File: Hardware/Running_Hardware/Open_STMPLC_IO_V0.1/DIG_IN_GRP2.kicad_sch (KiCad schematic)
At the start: 68 parts, among them J3 Screw_Terminal_01x04, J8 Screw_Terminal_01x04, U12 6N137, U20 6N137, U21 6N137, U22 6N137, U23 6N137, U24 6N137

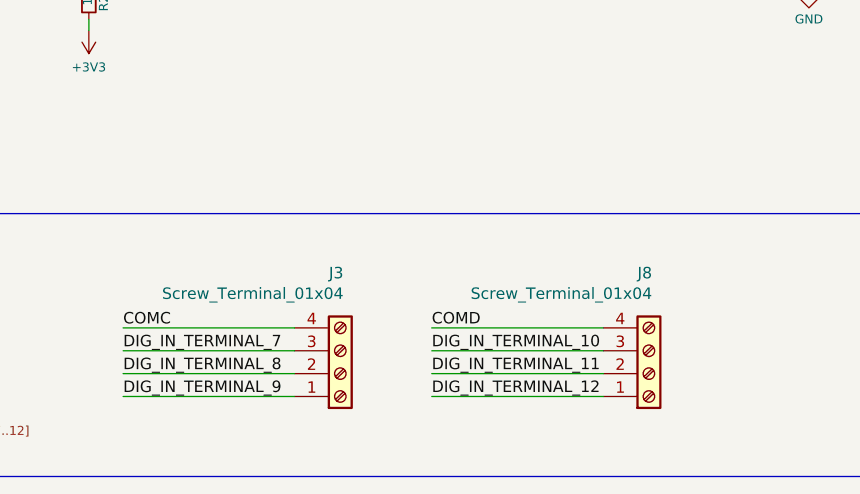
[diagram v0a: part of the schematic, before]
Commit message: Input circuit added
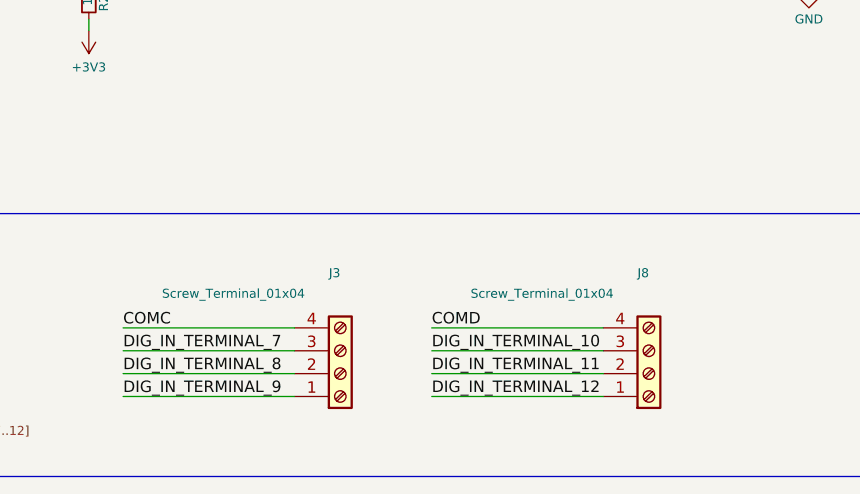
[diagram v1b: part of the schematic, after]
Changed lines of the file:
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@@
 			(effects
 				(font
-					(size 1.27 1.27)
+					(size 1 1)
 				)
 				(justify left)
@@
 			(effects
 				(font
-					(size 1.27 1.27)
+					(size 1 1)
 				)
 				(justify left)
@@
 			(effects
 				(font
-					(size 1.27 1.27)
+					(size 1 1)
 				)
 				(justify left)
@@
 			(effects
 				(font
-					(size 1.27 1.27)
+					(size 1 1)
 				)
 				(justify left)

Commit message: IO board layout
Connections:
- net COMC: now also J3.1 (Pin_1); no longer J3.4 (Pin_4)
- net COMD: now also J8.1 (Pin_1); no longer J8.4 (Pin_4)
- net DIG_IN_TERMINAL_10: now also J8.2 (Pin_2); no longer J8.3 (Pin_3)
- net DIG_IN_TERMINAL_11: now also J8.3 (Pin_3); no longer J8.2 (Pin_2)
- net DIG_IN_TERMINAL_12: now also J8.4 (Pin_4); no longer J8.1 (Pin_1)
- net DIG_IN_TERMINAL_7: now also J3.2 (Pin_2); no longer J3.3 (Pin_3)
- net DIG_IN_TERMINAL_8: now also J3.3 (Pin_3); no longer J3.2 (Pin_2)
- net DIG_IN_TERMINAL_9: now also J3.4 (Pin_4); no longer J3.1 (Pin_1)
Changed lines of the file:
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@@
 	(symbol
 		(lib_id "Connector:Screw_Terminal_01x04")
-		(at 113.03 182.88 0)
-		(mirror x)
+		(at 113.03 180.34 0)
 		(unit 1)
 		(exclude_from_sim no)
@@
 		(dnp no)
 		(property "Reference" "J3"
-			(at 111.76 171.704 0)
+			(at 111.76 191.516 0)
 			(effects
 				(font
@@
 		)
 		(property "Value" "Screw_Terminal_01x04"
-			(at 93.218 173.99 0)
+			(at 93.218 189.23 0)
 			(effects
 				(font
@@
 		)
 		(property "Footprint" "TerminalBlock_Phoenix:TerminalBlock_Phoenix_MKDS-1-4-3.81_1x04_P3.81mm_Horizontal"
-			(at 113.03 182.88 0)
+			(at 113.03 180.34 0)
 			(effects
 				(font
@@
 		)
 		(property "Datasheet" "~"
-			(at 113.03 182.88 0)
+			(at 113.03 180.34 0)
 			(effects
 				(font
@@
 		)
 		(property "Description" "Generic screw terminal, single row, 01x04, script generated (kicad-library-utils/schlib/autogen/connector/)"
-			(at 113.03 182.88 0)
+			(at 113.03 180.34 0)
 			(effects
 				(font
@@
 	(symbol
 		(lib_id "Connector:Screw_Terminal_01x04")
-		(at 147.32 182.88 0)
-		(mirror x)
+		(at 147.32 180.34 0)
 		(unit 1)
 		(exclude_from_sim no)
@@
 		(dnp no)
 		(property "Reference" "J8"
-			(at 146.05 171.704 0)
+			(at 146.05 191.516 0)
 			(effects
 				(font
@@
 		)
 		(property "Value" "Screw_Terminal_01x04"
-			(at 127.508 173.99 0)
+			(at 127.508 189.23 0)
 			(effects
 				(font
@@
 		)
 		(property "Footprint" "TerminalBlock_Phoenix:TerminalBlock_Phoenix_MKDS-1-4-3.81_1x04_P3.81mm_Horizontal"
-			(at 147.32 182.88 0)
+			(at 147.32 180.34 0)
 			(effects
 				(font
@@
 		)
 		(property "Datasheet" "~"
-			(at 147.32 182.88 0)
+			(at 147.32 180.34 0)
 			(effects
 				(font
@@
 		)
 		(property "Description" "Generic screw terminal, single row, 01x04, script generated (kicad-library-utils/schlib/autogen/connector/)"
-			(at 147.32 182.88 0)
-			(effects
-				(font
+			(at 147.32 180.34 0)
+			(effects
+				(font

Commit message: Main PCB changes
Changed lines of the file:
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@@
 		(effects
 			(font
-				(size 1.27 1.27)
+				(size 1 1)
 			)
 			(justify left bottom)
@@
 		(effects
 			(font
-				(size 1.27 1.27)
+				(size 1 1)
 			)
 			(justify right bottom)
@@
 		(effects
 			(font
-				(size 1.27 1.27)
+				(size 1 1)
 			)
 			(justify left bottom)
@@
 		(effects
 			(font
-				(size 1.27 1.27)
+				(size 1 1)
 			)
 			(justify right bottom)
@@
 		(effects
 			(font
-				(size 1.27 1.27)
+				(size 1 1)
 			)
 			(justify left bottom)
@@
 		(effects
 			(font
-				(size 1.27 1.27)
+				(size 1 1)
 			)
 			(justify left bottom)
@@
 		(effects
 			(font
-				(size 1.27 1.27)
+				(size 1 1)
 			)
 			(justify left bottom)
@@
 		(effects
 			(font
-				(size 1.27 1.27)
+				(size 1 1)
 			)
 			(justify left bottom)
@@
 		(effects
 			(font
-				(size 1.27 1.27)
+				(size 1 1)
 			)
 			(justify left bottom)
@@
 		(effects
 			(font
-				(size 1.27 1.27)
+				(size 1 1)
 			)
 			(justify right bottom)
@@
 		(effects
 			(font
-				(size 1.27 1.27)
+				(size 1 1)
 			)
 			(justify left bottom)
@@
 		(effects
 			(font
-				(size 1.27 1.27)
+				(size 1 1)
 			)
 			(justify left bottom)
@@
 		(effects
 			(font
-				(size 1.27 1.27)
+				(size 1 1)
 			)
 			(justify left bottom)
@@
 		(effects
 			(font
-				(size 1.27 1.27)
+				(size 1 1)
 			)
 			(justify right bottom)
@@
 		(effects
 			(font
-				(size 1.27 1.27)
+				(size 1 1)
 			)
 			(justify left bottom)
@@
 		(effects
 			(font
-				(size 1.27 1.27)
+				(size 1 1)
 			)
 			(justify right bottom)
@@
 		(effects
 			(font
-				(size 1.27 1.27)
+				(size 1 1)
 			)
 			(justify left bottom)
@@
 		(effects
 			(font
-				(size 1.27 1.27)
+				(size 1 1)
 			)
 			(justify left bottom)
@@
 		(effects
 			(font
-				(size 1.27 1.27)
+				(size 1 1)
 			)
 			(justify left bottom)
@@
 		(effects
 			(font
-				(size 1.27 1.27)
-			)
-			(justify right bottom)
+				(size 1 1)
+			)
+			(justify right bottom)

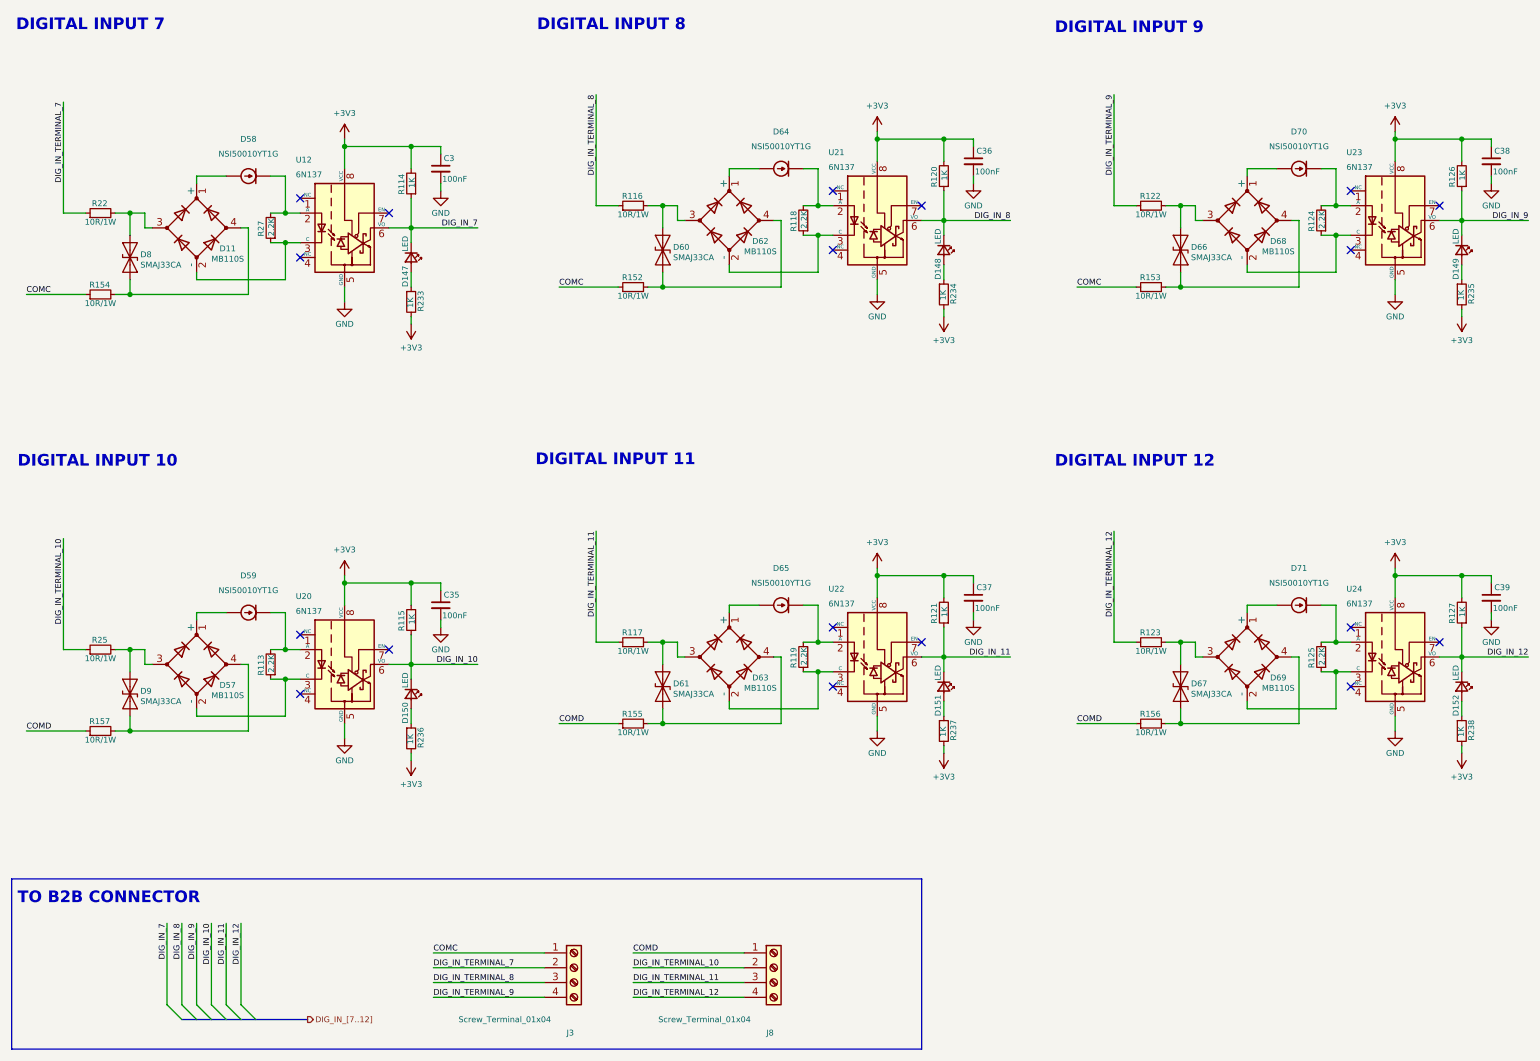
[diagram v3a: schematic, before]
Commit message: Schematic updates
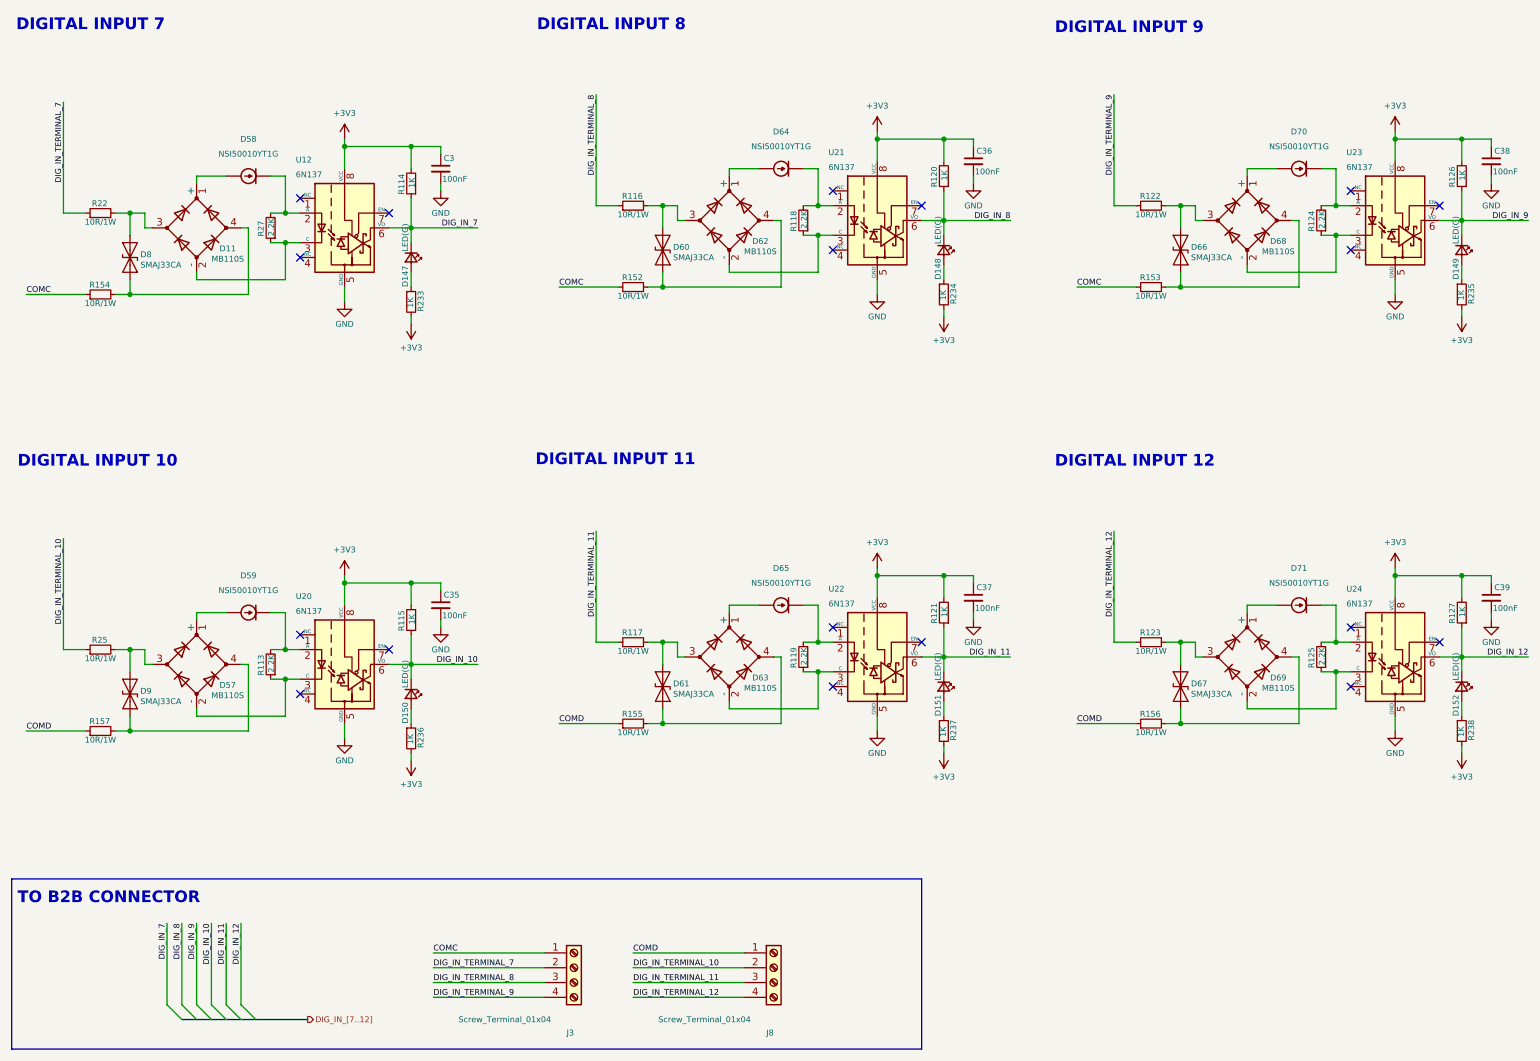
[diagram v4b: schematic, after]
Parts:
- D147, D148, D149, D150, D151, D152: value LED -> LED(G)
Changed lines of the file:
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@@
 			)
 		)
-		(property "Value" "LED"
+		(property "Value" "LED(G)"
 			(at 84.074 132.334 0)
 			(effects
@@
 			)
 		)
-		(property "Value" "LED"
+		(property "Value" "LED(G)"
 			(at 84.074 57.404 0)
 			(effects
@@
 			)
 		)
-		(property "Value" "LED"
+		(property "Value" "LED(G)"
 			(at 175.514 56.134 0)
 			(effects
@@
 			)
 		)
-		(property "Value" "LED"
+		(property "Value" "LED(G)"
 			(at 175.514 131.064 0)
 			(effects
@@
 			)
 		)
-		(property "Value" "LED"
+		(property "Value" "LED(G)"
 			(at 264.414 131.064 0)
 			(effects
@@
 			)
 		)
-		(property "Value" "LED"
+		(property "Value" "LED(G)"
 			(at 264.414 56.134 0)
 			(effects

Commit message: Gerber generation v0.1
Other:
- company: (none) -> Thingslista Automation LLP
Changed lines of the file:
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@@
 	(title_block
 		(title "Open_STMPLC_IO")
-		(date "2026-05-23")
+		(date "2026-06-03")
 		(rev "0.1")
+		(company "Thingslista Automation LLP")
 	)
 	(rectangle
